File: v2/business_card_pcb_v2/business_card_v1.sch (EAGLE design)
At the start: 74 parts, among them SW1 SPST_TACT-KMR2

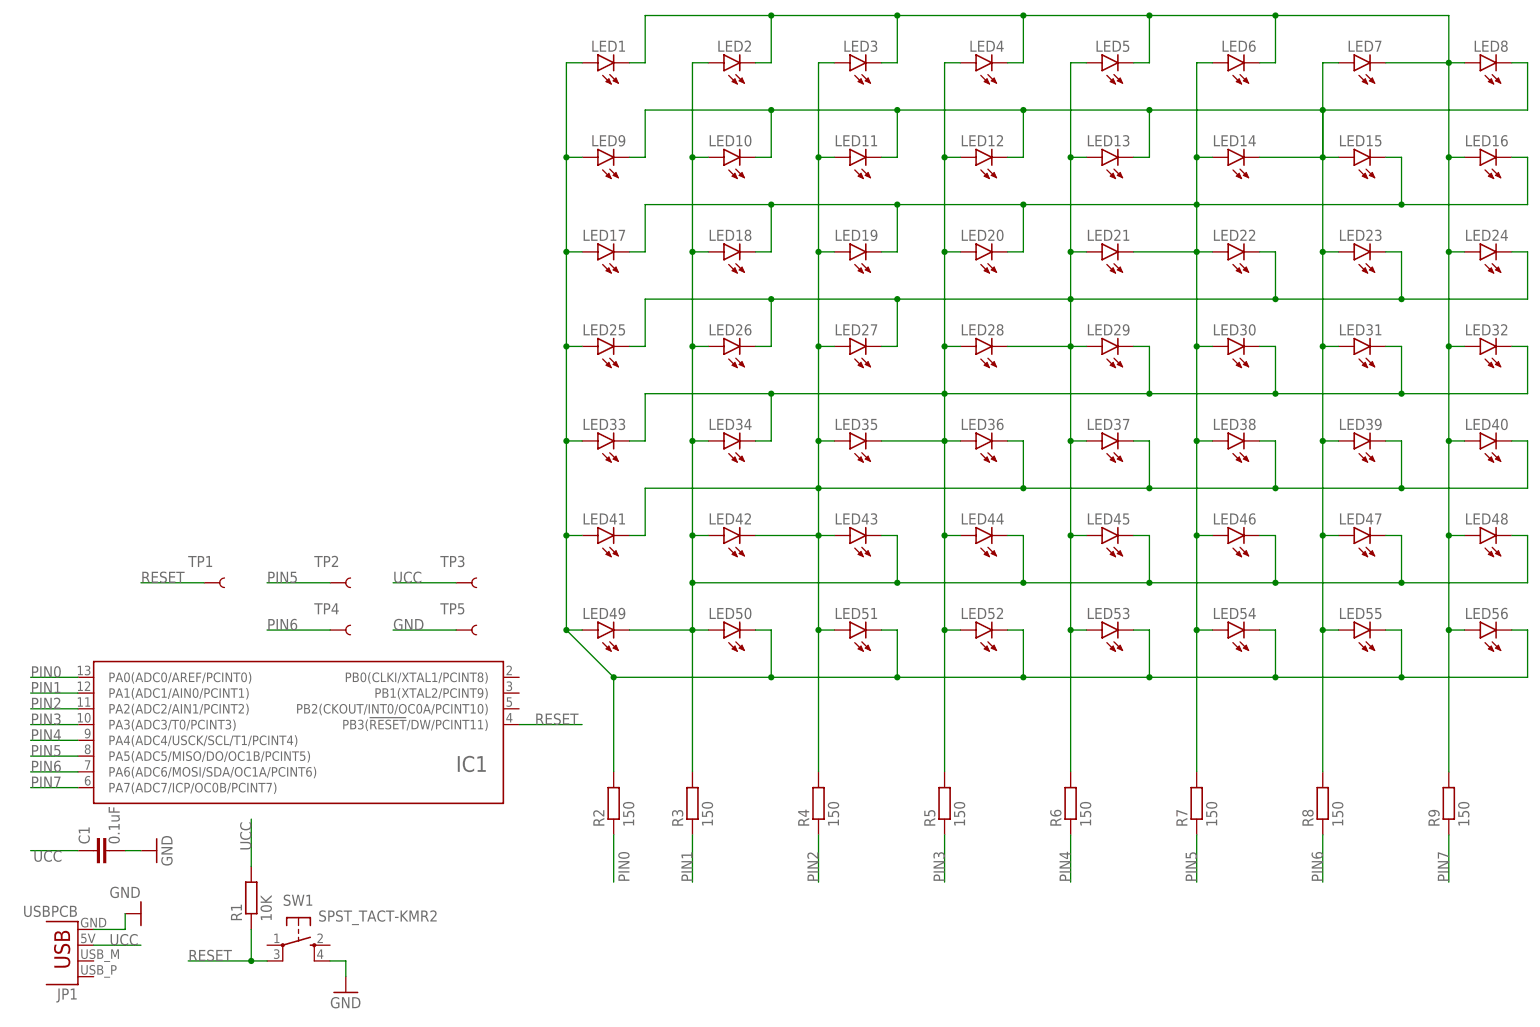
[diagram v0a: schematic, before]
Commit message: add the sck pad pin for miso and mosi
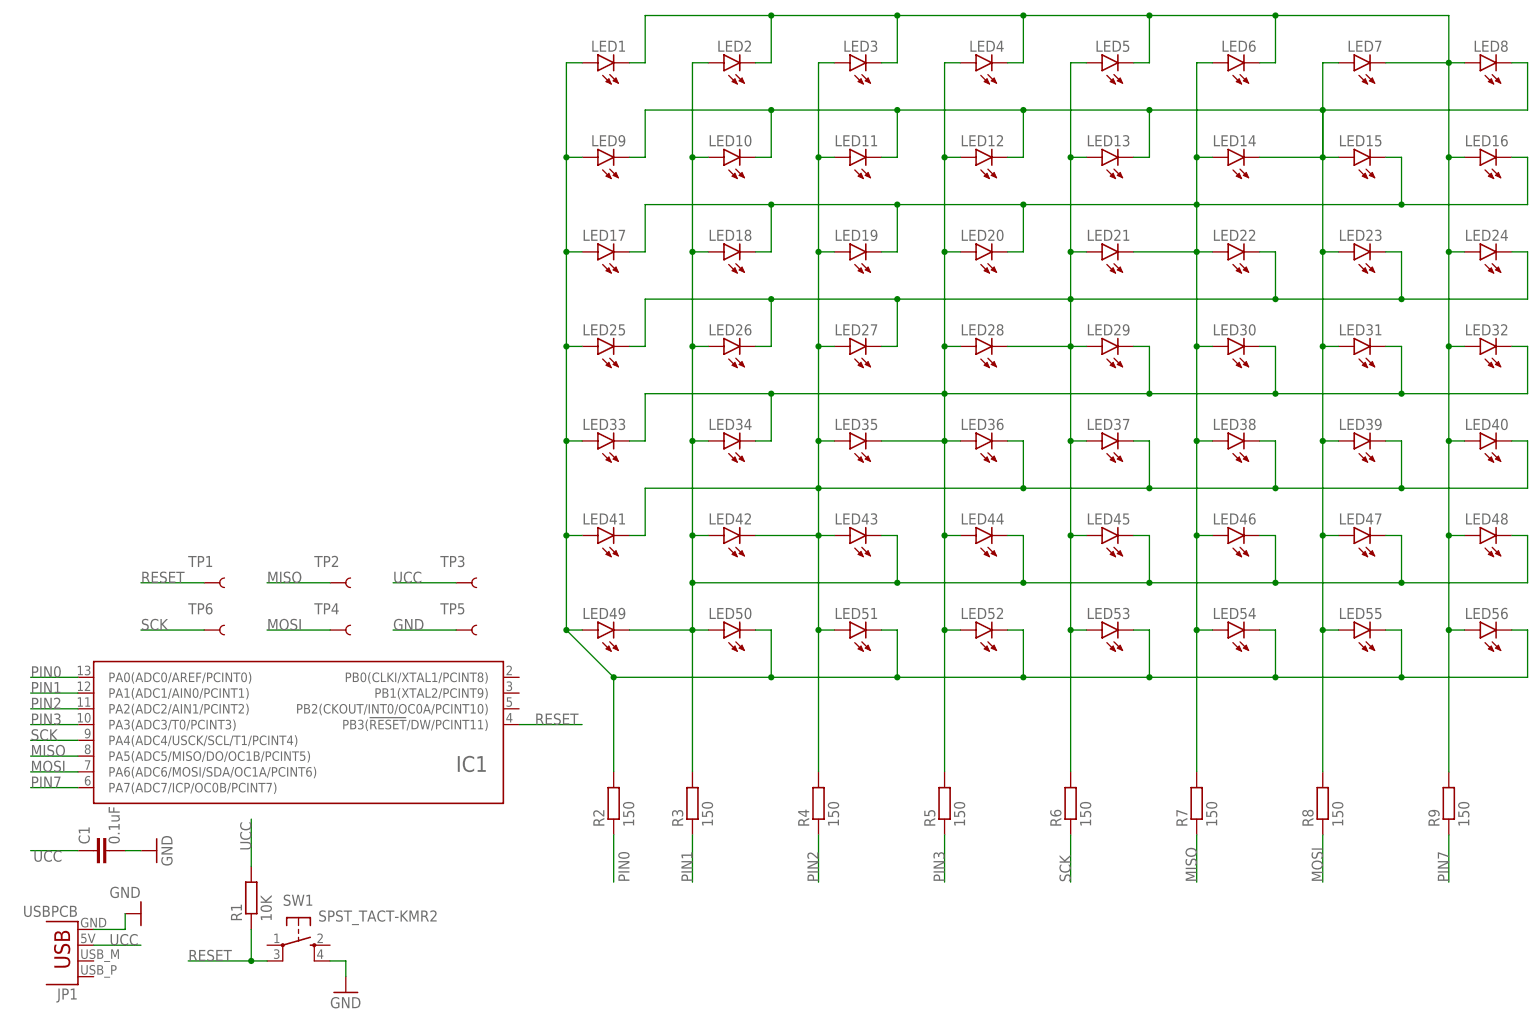
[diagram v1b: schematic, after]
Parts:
- added TP6: TEST-POINTPOGO_PTH, SparkFun-Connectors:TEST-POINTPOGO_PTH
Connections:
- net PIN5 renamed MISO
- net PIN6 renamed MOSI
- removed net PIN4: IC1IC.PA4(ADC4/USCK/SCL/T1/PCINT4), R6.1
- new net SCK: IC1IC.PA4(ADC4/USCK/SCL/T1/PCINT4), R6.1, TP6.1
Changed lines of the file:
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@@
 <part name="LED1" library="led" library_urn="urn:adsk.eagle:library:259" deviceset="LED" device="CHIPLED_0805" package3d_urn="urn:adsk.eagle:package:15821/2"/>
 <part name="SW1" library="adafruit" deviceset="SPST_TACT" device="-KMR2" package3d_urn="urn:adsk.eagle:package:17215455/2"/>
+<part name="TP6" library="SparkFun-Connectors" deviceset="TEST-POINT" device="POGO_PTH"/>
 </parts>
 <sheets>
@@
 <attribute name="VALUE" x="56.515" y="21.59" size="1.778" layer="96"/>
 </instance>
+<instance part="TP6" gate="G$1" x="38.1" y="68.58" smashed="yes">
+<attribute name="NAME" x="35.56" y="71.12" size="1.778" layer="95" font="vector"/>
+</instance>
 </instances>
 <busses>
@@
 <label x="10.16" y="53.34" size="1.778" layer="95"/>
 <pinref part="IC1" gate="IC" pin="PA3(ADC3/T0/PCINT3)"/>
-</segment>
-</net>
-<net name="PIN4" class="0">
-<segment>
-<wire x1="177.8" y1="27.94" x2="177.8" y2="35.56" width="0.1524" layer="91"/>
-<pinref part="R6" gate="G$1" pin="1"/>
-<label x="177.8" y="27.94" size="1.778" layer="95" rot="R90"/>
-</segment>
-<segment>
-<wire x1="17.78" y1="50.8" x2="10.16" y2="50.8" width="0.1524" layer="91"/>
-<label x="10.16" y="50.8" size="1.778" layer="95"/>
-<pinref part="IC1" gate="IC" pin="PA4(ADC4/USCK/SCL/T1/PCINT4)"/>
 </segment>
 </net>
@@
 </segment>
 </net>
-<net name="PIN5" class="0">
+<net name="PIN7" class="0">
+<segment>
+<wire x1="17.78" y1="43.18" x2="10.16" y2="43.18" width="0.1524" layer="91"/>
+<label x="10.16" y="43.18" size="1.778" layer="95"/>
+<pinref part="IC1" gate="IC" pin="PA7(ADC7/ICP/OC0B/PCINT7)"/>
+</segment>
+<segment>
+<pinref part="R9" gate="G$1" pin="1"/>
+<wire x1="238.76" y1="35.56" x2="238.76" y2="27.94" width="0.1524" layer="91"/>
+<label x="238.76" y="27.94" size="1.778" layer="95" rot="R90"/>
+</segment>
+</net>
+<net name="UCC" class="0">
+<segment>
+<pinref part="JP1" gate="G$1" pin="VBUS"/>
+<wire x1="20.32" y1="17.78" x2="27.94" y2="17.78" width="0.1524" layer="91"/>
+<label x="22.86" y="17.78" size="1.778" layer="95"/>
+</segment>
+<segment>
+<pinref part="C1" gate="G$1" pin="1"/>
+<wire x1="17.78" y1="33.02" x2="10.16" y2="33.02" width="0.1524" layer="91"/>
+<label x="15.24" y="33.02" size="1.778" layer="95" rot="R180"/>
+</segment>
+<segment>
+<pinref part="R1" gate="G$1" pin="2"/>
+<wire x1="45.72" y1="30.48" x2="45.72" y2="38.1" width="0.1524" layer="91"/>
+<label x="45.72" y="33.02" size="1.778" layer="95" rot="R90"/>
+</segment>
+<segment>
+<wire x1="78.74" y1="76.2" x2="68.58" y2="76.2" width="0.1524" layer="91"/>
+<label x="68.58" y="76.2" size="1.778" layer="95"/>
+<pinref part="TP3" gate="G$1" pin="1"/>
+</segment>
+</net>
+<net name="MISO" class="0">
+<segment>
+<wire x1="17.78" y1="48.26" x2="10.16" y2="48.26" width="0.1524" layer="91"/>
+<label x="10.16" y="48.26" size="1.778" layer="95"/>
+<pinref part="IC1" gate="IC" pin="PA5(ADC5/MISO/DO/OC1B/PCINT5)"/>
+</segment>
+<segment>
+<wire x1="58.42" y1="76.2" x2="48.26" y2="76.2" width="0.1524" layer="91"/>
+<label x="48.26" y="76.2" size="1.778" layer="95"/>
+<pinref part="TP2" gate="G$1" pin="1"/>
+</segment>
 <segment>
 <pinref part="R7" gate="G$1" pin="1"/>
@@
 <label x="198.12" y="27.94" size="1.778" layer="95" rot="R90"/>
 </segment>
-<segment>
-<wire x1="17.78" y1="48.26" x2="10.16" y2="48.26" width="0.1524" layer="91"/>
-<label x="10.16" y="48.26" size="1.778" layer="95"/>
-<pinref part="IC1" gate="IC" pin="PA5(ADC5/MISO/DO/OC1B/PCINT5)"/>
-</segment>
-<segment>
-<wire x1="58.42" y1="76.2" x2="48.26" y2="76.2" width="0.1524" layer="91"/>
-<label x="48.26" y="76.2" size="1.778" layer="95"/>
-<pinref part="TP2" gate="G$1" pin="1"/>
-</segment>
-</net>
-<net name="PIN6" class="0">
+</net>
+<net name="MOSI" class="0">
+<segment>
+<wire x1="17.78" y1="45.72" x2="10.16" y2="45.72" width="0.1524" layer="91"/>
+<label x="10.16" y="45.72" size="1.778" layer="95"/>
+<pinref part="IC1" gate="IC" pin="PA6(ADC6/MOSI/SDA/OC1A/PCINT6)"/>
+</segment>
+<segment>
+<wire x1="58.42" y1="68.58" x2="48.26" y2="68.58" width="0.1524" layer="91"/>
+<label x="48.26" y="68.58" size="1.778" layer="95"/>
+<pinref part="TP4" gate="G$1" pin="1"/>
+</segment>
 <segment>
 <pinref part="R8" gate="G$1" pin="1"/>
@@
 <label x="218.44" y="27.94" size="1.778" layer="95" rot="R90"/>
 </segment>
-<segment>
-<wire x1="17.78" y1="45.72" x2="10.16" y2="45.72" width="0.1524" layer="91"/>
-<label x="10.16" y="45.72" size="1.778" layer="95"/>
-<pinref part="IC1" gate="IC" pin="PA6(ADC6/MOSI/SDA/OC1A/PCINT6)"/>
-</segment>
-<segment>
-<wire x1="58.42" y1="68.58" x2="48.26" y2="68.58" width="0.1524" layer="91"/>
-<label x="48.26" y="68.58" size="1.778" layer="95"/>
-<pinref part="TP4" gate="G$1" pin="1"/>
-</segment>
-</net>
-<net name="PIN7" class="0">
-<segment>
-<pinref part="R9" gate="G$1" pin="1"/>
-<wire x1="238.76" y1="35.56" x2="238.76" y2="27.94" width="0.1524" layer="91"/>
-<label x="238.76" y="27.94" size="1.778" layer="95" rot="R90"/>
-</segment>
-<segment>
-<wire x1="17.78" y1="43.18" x2="10.16" y2="43.18" width="0.1524" layer="91"/>
-<label x="10.16" y="43.18" size="1.778" layer="95"/>
-<pinref part="IC1" gate="IC" pin="PA7(ADC7/ICP/OC0B/PCINT7)"/>
-</segment>
-</net>
-<net name="UCC" class="0">
-<segment>
-<pinref part="JP1" gate="G$1" pin="VBUS"/>
-<wire x1="20.32" y1="17.78" x2="27.94" y2="17.78" width="0.1524" layer="91"/>
-<label x="22.86" y="17.78" size="1.778" layer="95"/>
-</segment>
-<segment>
-<pinref part="C1" gate="G$1" pin="1"/>
-<wire x1="17.78" y1="33.02" x2="10.16" y2="33.02" width="0.1524" layer="91"/>
-<label x="15.24" y="33.02" size="1.778" layer="95" rot="R180"/>
-</segment>
-<segment>
-<pinref part="R1" gate="G$1" pin="2"/>
-<wire x1="45.72" y1="30.48" x2="45.72" y2="38.1" width="0.1524" layer="91"/>
-<label x="45.72" y="33.02" size="1.778" layer="95" rot="R90"/>
-</segment>
-<segment>
-<wire x1="78.74" y1="76.2" x2="68.58" y2="76.2" width="0.1524" layer="91"/>
-<label x="68.58" y="76.2" size="1.778" layer="95"/>
-<pinref part="TP3" gate="G$1" pin="1"/>
-</segment>
-</net>
+</net>
+<net name="SCK" class="0">
+<segment>
+<wire x1="17.78" y1="50.8" x2="10.16" y2="50.8" width="0.1524" layer="91"/>
+<label x="10.16" y="50.8" size="1.778" layer="95"/>
+<pinref part="IC1" gate="IC" pin="PA4(ADC4/USCK/SCL/T1/PCINT4)"/>
+</segment>
+<segment>
+<pinref part="TP6" gate="G$1" pin="1"/>
+<wire x1="38.1" y1="68.58" x2="27.94" y2="68.58" width="0.1524" layer="91"/>
+<label x="27.94" y="68.58" size="1.778" layer="95"/>
+</segment>
+<segment>
+<wire x1="177.8" y1="27.94" x2="177.8" y2="35.56" width="0.1524" layer="91"/>
+<pinref part="R6" gate="G$1" pin="1"/>
+<label x="177.8" y="27.94" size="1.778" layer="95" rot="R90"/>
+</segment>
+</net>
